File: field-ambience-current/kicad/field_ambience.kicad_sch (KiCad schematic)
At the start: 0 parts

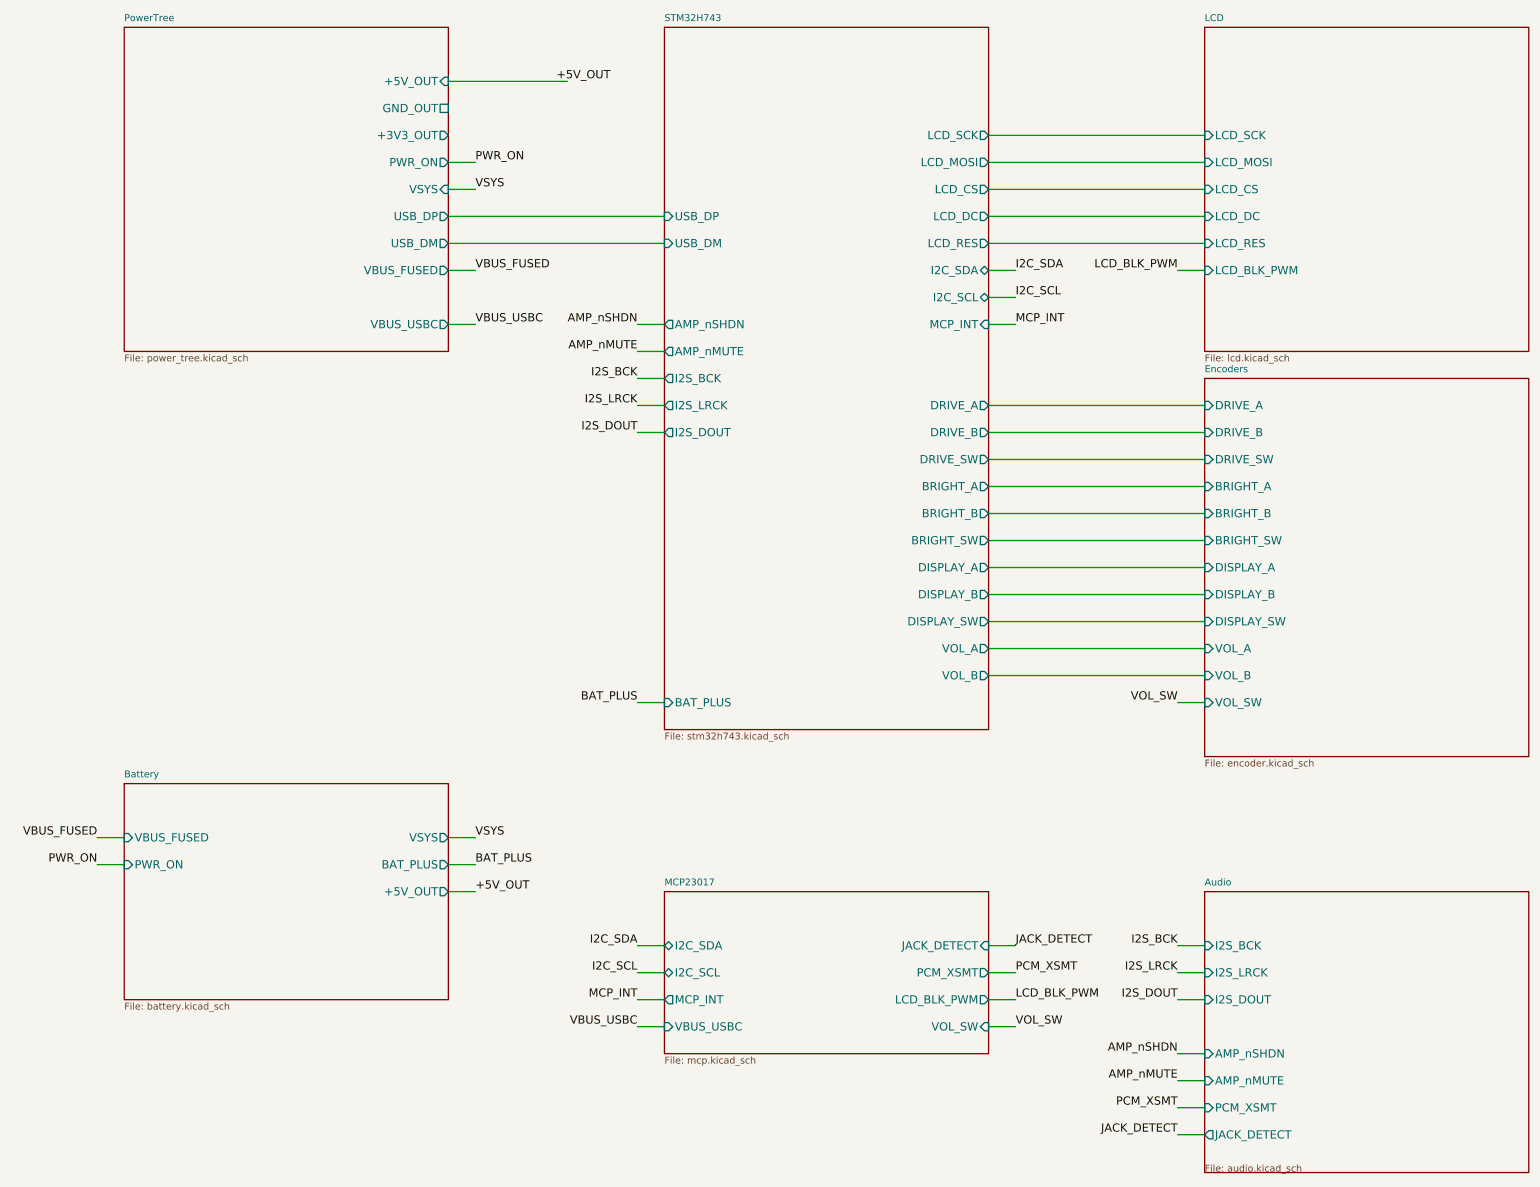
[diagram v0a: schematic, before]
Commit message: hw(audit): BOM/Schematic-Audit Runde 2 — Symbol-Leichen, 17 ERC-Konflikte, Netznamen (r19.64)
Ausgeloest von Arons 40-Pin-Rueckfrage. Die BOM selbst ist byte-identisch
geblieben (kein Bauteil, kein LCSC-Code, keine Menge geaendert).

1) Symbol-Leichen — dieselbe Ursache wie die 40-Pin-Frage
   Drei weitere Symbole waren in der eingebetteten Library JEDES Sheets
   definiert, aber nirgends platziert:
     - MCU:Pico2 (laut Generator ein "40-pin module symbol" — zweite
       moegliche Quelle von Arons Sichtung)
     - Connector:Conn_01x16 (OLED-Aera)
     - Transistor_FET:DMG2305UX (Q1-Power-Path, r18.79 entfernt)
   Dazu die toten Generator-Funktionen pico_sheet(), oled_sheet(),
   _conn_02xN_lib_symbol() (~880 Zeilen). Gegenprobe: Library == exakt 37
   Symbole == exakt 37 platzierte lib_ids, null Waisen in beide Richtungen.
   Diff pro Sheet: 210 Loeschungen, 0 Zusaetze. jlc_bom.csv md5 unveraendert.

2) ERC: 17 Sheet-Pin/Hier-Label-Richtungskonflikte
   - 11x Encoder (DRIVE/BRIGHT/DISPLAY/VOL): das STM32-Sheet deklarierte sie
     als output, obwohl die MCU sie liest — Encoder- und MCU-Sheet trieben
     beide dasselbe Netz. MCU-Seite jetzt input, Encoder-Root-Pin output.
   - VOL_SW: Root input vs. Sheet output.
   - USB_DP/DM: dreimal unterschiedlich -> durchgaengig bidirectional.
   - I2C_SCL/SDA: Slave-Sheets input vs. Root bidirectional -> bidirectional.
   - VSYS: das Battery-Sheet hatte zwei zusaetzliche Hier-Labels fuer
     sheet-INTERNE Verbraucher (L1, U8-VIN) ohne Root-Sheet-Pin -> jetzt
     normale lokale Labels. Netz-Topologie unveraendert.
   Alle 7 Sheets: Root-Pins == Hier-Labels, 0 Diffs.

3) Netznamen gegen AI_READY_SCHEMATIC_STANDARD
   - GPA5/XSMT und GPA6/JACKDET: Slash im Netznamen (verboten; '/' ist in
     KiCad der Hierarchie-Pfadtrenner) und doppelte Benennung eines Netzes,
     das ueber PCM_XSMT / JACK_DETECT schon benannt war. Entfernt.
   - Active-Low auf die geforderte _N-Endung: AMP_nSHDN -> AMP_SHDN_N,
     AMP_nMUTE -> AMP_MUTE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
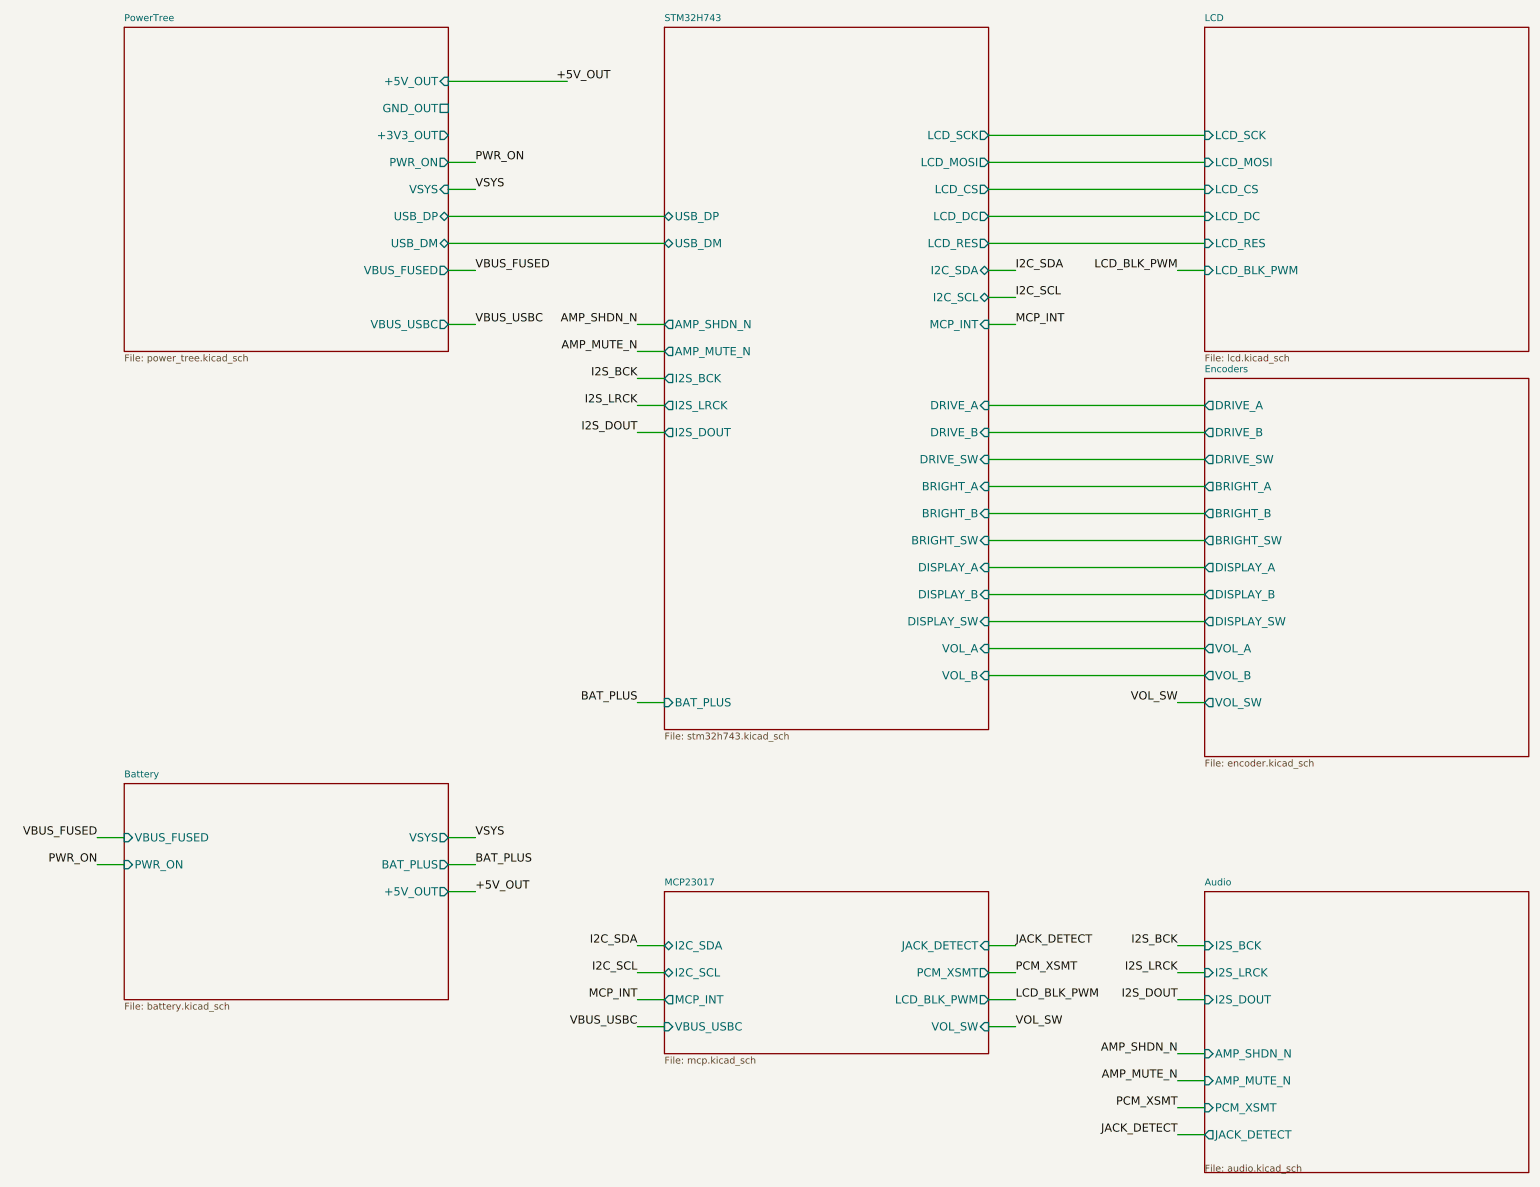
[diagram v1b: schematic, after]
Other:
- sheet Audio ports: added AMP_MUTE_N, AMP_SHDN_N; removed AMP_nMUTE, AMP_nSHDN
- sheet STM32H743 ports: added AMP_MUTE_N, AMP_SHDN_N; removed AMP_nMUTE, AMP_nSHDN
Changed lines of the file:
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@@
       (effects (font (size 1.524 1.524)) (justify right))
 )
-    (pin "USB_DP" output (at 90 75 0)
-      (effects (font (size 1.524 1.524)) (justify right))
-)
-    (pin "USB_DM" output (at 90 80 0)
+    (pin "USB_DP" bidirectional (at 90 75 0)
+      (effects (font (size 1.524 1.524)) (justify right))
+)
+    (pin "USB_DM" bidirectional (at 90 80 0)
       (effects (font (size 1.524 1.524)) (justify right))
 )
@@
     (property "Sheetfile" "stm32h743.kicad_sch" (at 130 170.5 0)
       (effects (font (size 1.27 1.27)) (justify left top)))
-    (pin "USB_DP" input (at 130 75 180)
-      (effects (font (size 1.524 1.524)) (justify left))
-)
-    (pin "USB_DM" input (at 130 80 180)
+    (pin "USB_DP" bidirectional (at 130 75 180)
+      (effects (font (size 1.524 1.524)) (justify left))
+)
+    (pin "USB_DM" bidirectional (at 130 80 180)
       (effects (font (size 1.524 1.524)) (justify left))
 )
@@
       (effects (font (size 1.524 1.524)) (justify right))
 )
-    (pin "DRIVE_A" output (at 190 110 0)
-      (effects (font (size 1.524 1.524)) (justify right))
-)
-    (pin "DRIVE_B" output (at 190 115 0)
-      (effects (font (size 1.524 1.524)) (justify right))
-)
-    (pin "DRIVE_SW" output (at 190 120 0)
-      (effects (font (size 1.524 1.524)) (justify right))
-)
-    (pin "BRIGHT_A" output (at 190 125 0)
-      (effects (font (size 1.524 1.524)) (justify right))
-)
-    (pin "BRIGHT_B" output (at 190 130 0)
-      (effects (font (size 1.524 1.524)) (justify right))
-)
-    (pin "BRIGHT_SW" output (at 190 135 0)
-      (effects (font (size 1.524 1.524)) (justify right))
-)
-    (pin "DISPLAY_A" output (at 190 140 0)
-      (effects (font (size 1.524 1.524)) (justify right))
-)
-    (pin "DISPLAY_B" output (at 190 145 0)
-      (effects (font (size 1.524 1.524)) (justify right))
-)
-    (pin "DISPLAY_SW" output (at 190 150 0)
-      (effects (font (size 1.524 1.524)) (justify right))
-)
-    (pin "VOL_A" output (at 190 155 0)
-      (effects (font (size 1.524 1.524)) (justify right))
-)
-    (pin "VOL_B" output (at 190 160 0)
-      (effects (font (size 1.524 1.524)) (justify right))
-)
-    (pin "AMP_nSHDN" output (at 130 95 180)
-      (effects (font (size 1.524 1.524)) (justify left))
-)
-    (pin "AMP_nMUTE" output (at 130 100 180)
+    (pin "DRIVE_A" input (at 190 110 0)
+      (effects (font (size 1.524 1.524)) (justify right))
+)
+    (pin "DRIVE_B" input (at 190 115 0)
+      (effects (font (size 1.524 1.524)) (justify right))
+)
+    (pin "DRIVE_SW" input (at 190 120 0)
+      (effects (font (size 1.524 1.524)) (justify right))
+)
+    (pin "BRIGHT_A" input (at 190 125 0)
+      (effects (font (size 1.524 1.524)) (justify right))
+)
+    (pin "BRIGHT_B" input (at 190 130 0)
+      (effects (font (size 1.524 1.524)) (justify right))
+)
+    (pin "BRIGHT_SW" input (at 190 135 0)
+      (effects (font (size 1.524 1.524)) (justify right))
+)
+    (pin "DISPLAY_A" input (at 190 140 0)
+      (effects (font (size 1.524 1.524)) (justify right))
+)
+    (pin "DISPLAY_B" input (at 190 145 0)
+      (effects (font (size 1.524 1.524)) (justify right))
+)
+    (pin "DISPLAY_SW" input (at 190 150 0)
+      (effects (font (size 1.524 1.524)) (justify right))
+)
+    (pin "VOL_A" input (at 190 155 0)
+      (effects (font (size 1.524 1.524)) (justify right))
+)
+    (pin "VOL_B" input (at 190 160 0)
+      (effects (font (size 1.524 1.524)) (justify right))
+)
+    (pin "AMP_SHDN_N" output (at 130 95 180)
+      (effects (font (size 1.524 1.524)) (justify left))
+)
+    (pin "AMP_MUTE_N" output (at 130 100 180)
       (effects (font (size 1.524 1.524)) (justify left))
 )
@@
     (property "Sheetfile" "encoder.kicad_sch" (at 230 175.5 0)
       (effects (font (size 1.27 1.27)) (justify left top)))
-    (pin "DRIVE_A" input (at 230 110 180)
-      (effects (font (size 1.524 1.524)) (justify left))
-)
-    (pin "DRIVE_B" input (at 230 115 180)
-      (effects (font (size 1.524 1.524)) (justify left))
-)
-    (pin "DRIVE_SW" input (at 230 120 180)
-      (effects (font (size 1.524 1.524)) (justify left))
-)
-    (pin "BRIGHT_A" input (at 230 125 180)
-      (effects (font (size 1.524 1.524)) (justify left))
-)
-    (pin "BRIGHT_B" input (at 230 130 180)
-      (effects (font (size 1.524 1.524)) (justify left))
-)
-    (pin "BRIGHT_SW" input (at 230 135 180)
-      (effects (font (size 1.524 1.524)) (justify left))
-)
-    (pin "DISPLAY_A" input (at 230 140 180)
-      (effects (font (size 1.524 1.524)) (justify left))
-)
-    (pin "DISPLAY_B" input (at 230 145 180)
-      (effects (font (size 1.524 1.524)) (justify left))
-)
-    (pin "DISPLAY_SW" input (at 230 150 180)
-      (effects (font (size 1.524 1.524)) (justify left))
-)
-    (pin "VOL_A" input (at 230 155 180)
-      (effects (font (size 1.524 1.524)) (justify left))
-)
-    (pin "VOL_B" input (at 230 160 180)
-      (effects (font (size 1.524 1.524)) (justify left))
-)
-    (pin "VOL_SW" input (at 230 165 180)
+    (pin "DRIVE_A" output (at 230 110 180)
+      (effects (font (size 1.524 1.524)) (justify left))
+)
+    (pin "DRIVE_B" output (at 230 115 180)
+      (effects (font (size 1.524 1.524)) (justify left))
+)
+    (pin "DRIVE_SW" output (at 230 120 180)
+      (effects (font (size 1.524 1.524)) (justify left))
+)
+    (pin "BRIGHT_A" output (at 230 125 180)
+      (effects (font (size 1.524 1.524)) (justify left))
+)
+    (pin "BRIGHT_B" output (at 230 130 180)
+      (effects (font (size 1.524 1.524)) (justify left))
+)
+    (pin "BRIGHT_SW" output (at 230 135 180)
+      (effects (font (size 1.524 1.524)) (justify left))
+)
+    (pin "DISPLAY_A" output (at 230 140 180)
+      (effects (font (size 1.524 1.524)) (justify left))
+)
+    (pin "DISPLAY_B" output (at 230 145 180)
+      (effects (font (size 1.524 1.524)) (justify left))
+)
+    (pin "DISPLAY_SW" output (at 230 150 180)
+      (effects (font (size 1.524 1.524)) (justify left))
+)
+    (pin "VOL_A" output (at 230 155 180)
+      (effects (font (size 1.524 1.524)) (justify left))
+)
+    (pin "VOL_B" output (at 230 160 180)
+      (effects (font (size 1.524 1.524)) (justify left))
+)
+    (pin "VOL_SW" output (at 230 165 180)
       (effects (font (size 1.524 1.524)) (justify left))
 ))
@@
       (effects (font (size 1.524 1.524)) (justify left))
 )
-    (pin "AMP_nSHDN" input (at 230 230 180)
-      (effects (font (size 1.524 1.524)) (justify left))
-)
-    (pin "AMP_nMUTE" input (at 230 235 180)
+    (pin "AMP_SHDN_N" input (at 230 230 180)
+      (effects (font (size 1.524 1.524)) (justify left))
+)
+    (pin "AMP_MUTE_N" input (at 230 235 180)
       (effects (font (size 1.524 1.524)) (justify left))
 )
@@
   (label "+5V_OUT" (at 110 50 0) (effects (font (size 1.524 1.524)) (justify left bottom)))
   (wire (pts (xy 125 95) (xy 130 95)) (stroke (width 0) (type default)))
-  (label "AMP_nSHDN" (at 125 95 0) (effects (font (size 1.524 1.524)) (justify right bottom)))
+  (label "AMP_SHDN_N" (at 125 95 0) (effects (font (size 1.524 1.524)) (justify right bottom)))
   (wire (pts (xy 125 100) (xy 130 100)) (stroke (width 0) (type default)))
-  (label "AMP_nMUTE" (at 125 100 0) (effects (font (size 1.524 1.524)) (justify right bottom)))
+  (label "AMP_MUTE_N" (at 125 100 0) (effects (font (size 1.524 1.524)) (justify right bottom)))
   (wire (pts (xy 225 230) (xy 230 230)) (stroke (width 0) (type default)))
-  (label "AMP_nSHDN" (at 225 230 0) (effects (font (size 1.524 1.524)) (justify right bottom)))
+  (label "AMP_SHDN_N" (at 225 230 0) (effects (font (size 1.524 1.524)) (justify right bottom)))
   (wire (pts (xy 225 235) (xy 230 235)) (stroke (width 0) (type default)))
-  (label "AMP_nMUTE" (at 225 235 0) (effects (font (size 1.524 1.524)) (justify right bottom)))
+  (label "AMP_MUTE_N" (at 225 235 0) (effects (font (size 1.524 1.524)) (justify right bottom)))
   (wire (pts (xy 190 215) (xy 195 215)) (stroke (width 0) (type default)))
   (label "PCM_XSMT" (at 195 215 0) (effects (font (size 1.524 1.524)) (justify left bottom)))
